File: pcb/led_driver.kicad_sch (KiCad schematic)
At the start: 60 parts, among them J1 48V IN, J2 LED, J3 12V IN, J4 INTERLOCK, Q1 IRF540N, SW3 ARM, U1 TC4427xOA, U2 74HC74, U3 74HC08, U4 LM393

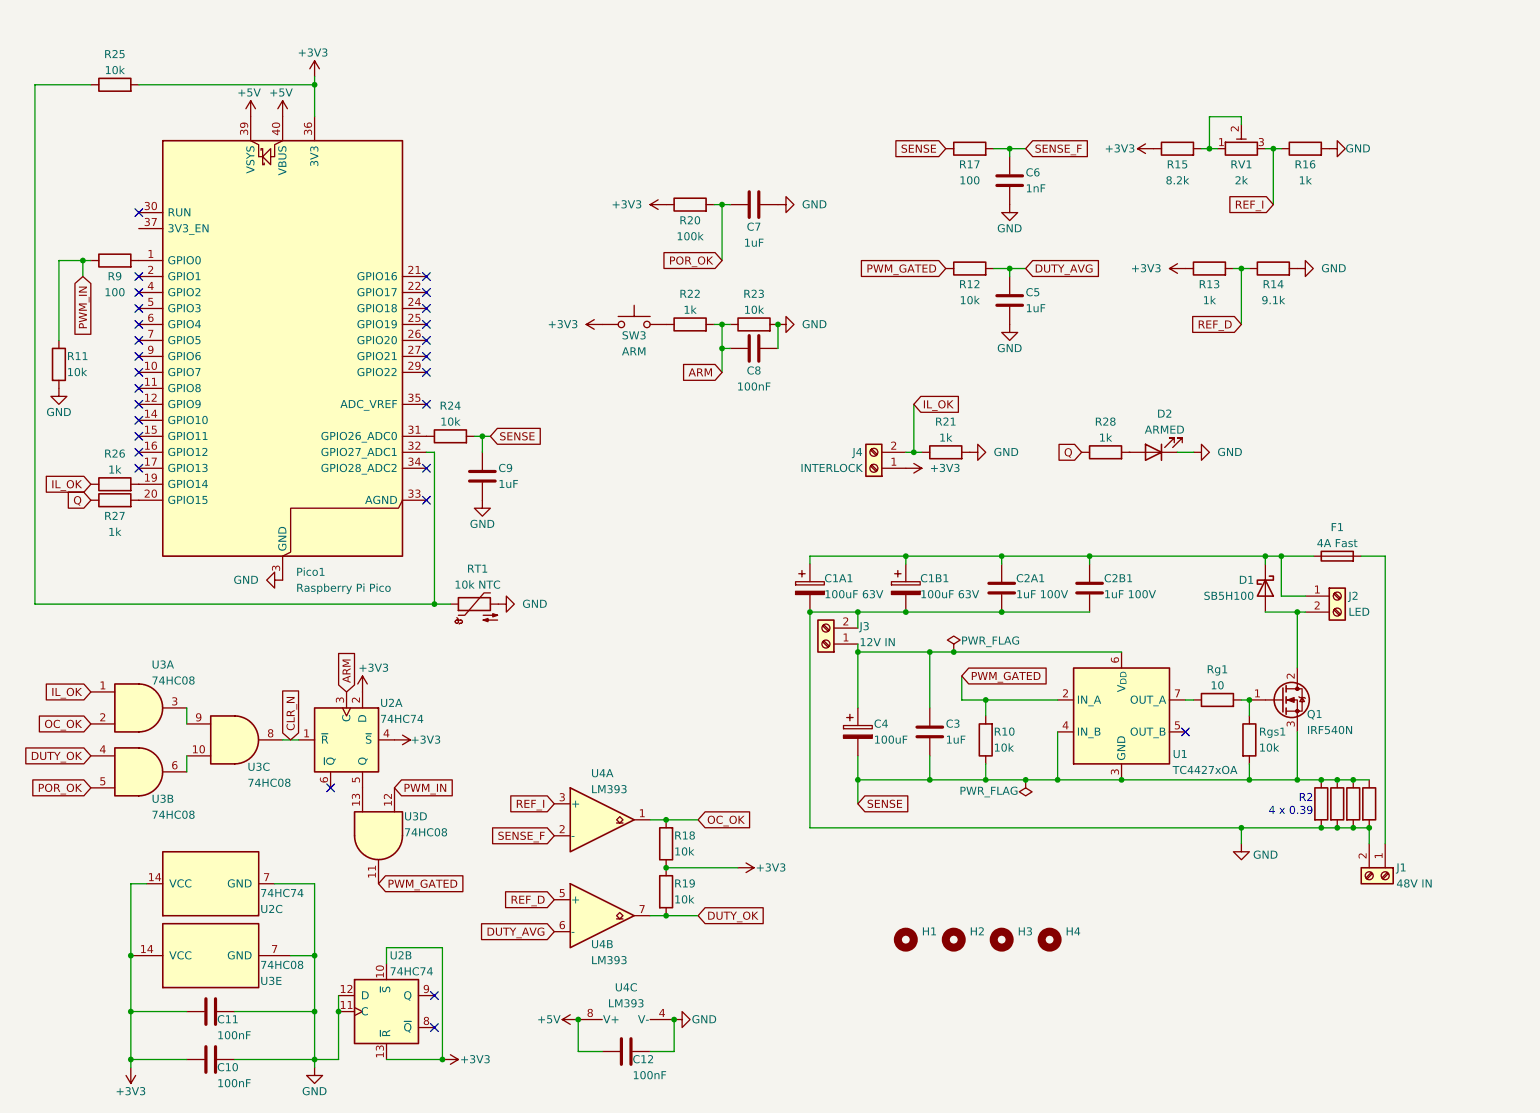
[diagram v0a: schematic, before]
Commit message: Initial routing for LED driver
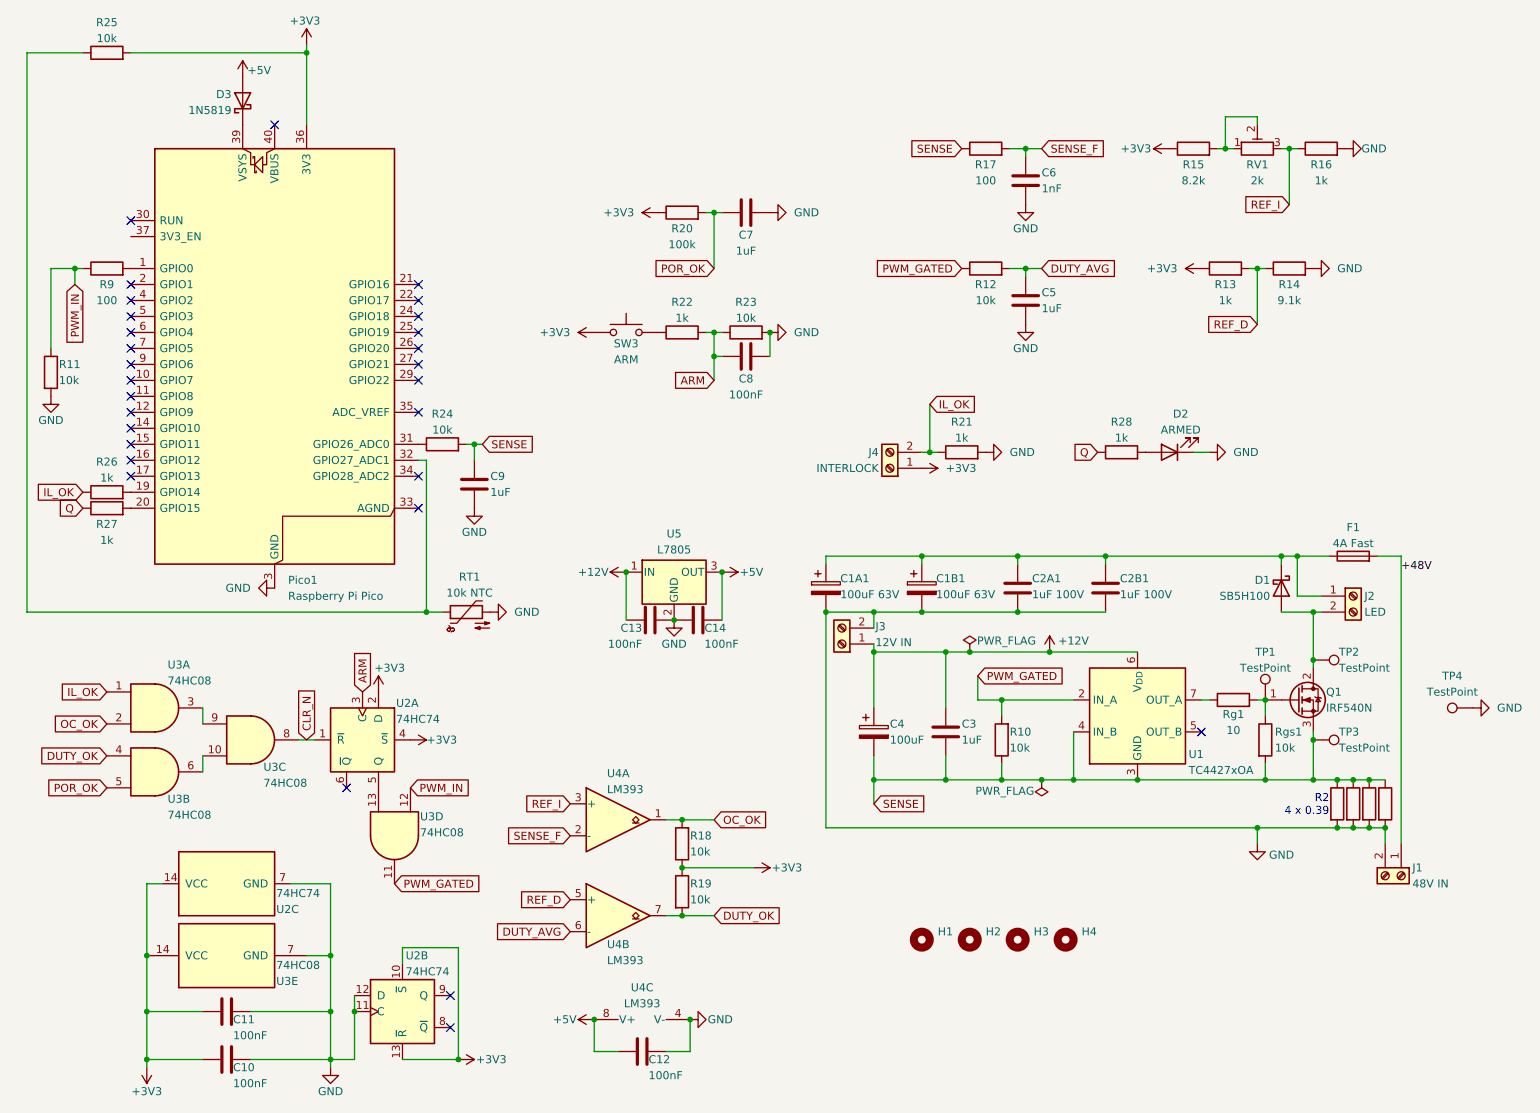
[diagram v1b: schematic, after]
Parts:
- added C13, C14: 100nF, Capacitor_THT:C_Rect_L7.2mm_W4.5mm_P5.00mm_FKS2_FKP2_MKS2_MKP2, symbol Device:C
- added D3: 1N5819, Diode_THT:D_DO-41_SOD81_P10.16mm_Horizontal, symbol Diode:1N5819
- added TP1, TP2, TP3, TP4: TestPoint, TestPoint:TestPoint_THTPad_D2.0mm_Drill1.0mm, symbol Connector:TestPoint
- added U5: L7805, Package_TO_SOT_THT:TO-220-3_Vertical, symbol Regulator_Linear:L7805
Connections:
- net +5V: now also C14.2, D3.2 (A), U5.3 (OUT); no longer Pico1.39 (VSYS), Pico1.40 (VBUS)
- net GND: now also C13.2, C14.1, TP4.1, U5.2 (GND)
- net SENSE: now also TP3.1
- net at Q1.1 (G), Rg1.2, Rgs1.1: now also TP1.1
- net at D1.2 (A), J2.2 (Pin_2), Q1.2 (D): now also TP2.1
- net +48V: now reaches F1.2, J1.1 (Pin_1)
- net +12V: now reaches C3.1, C4.1, J3.1 (Pin_1), U1.6 (V_{DD})
- net +12V: now also C13.1, U5.1 (IN)
- new net: D3.1 (K), Pico1.39 (VSYS)
- no-connect marks 28 -> 29
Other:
- moved on the sheet: C10, C11, C12, C1A1, C1B1, C2A1, C2B1, C3, C4, C5, C6, C7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

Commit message: Fix some constraint error and violations
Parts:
- added R29: 10k, Resistor_THT:R_Axial_DIN0207_L6.3mm_D2.5mm_P10.16mm_Horizontal, symbol Device:R
- Q1: value IRF540N -> STP30NF10
- R13: value 1k -> 10k
- R14: value 9.1k -> 8.2k
- Rgs1: footprint Resistor_THT:R_Axial_DIN0207_L6.3mm_D2.5mm_P10.16mm_Horizontal -> Resistor_THT:R_Axial_DIN0207_L6.3mm_D2.5mm_P2.54mm_Vertical
- U1: value TC4427xOA -> MIC4427
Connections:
- net DUTY_AVG: now also R29.1
- net GND: now also C3.2, C4.2, R10.1, U1.3 (GND), U1.4 (IN_B), R29.2
- net Q: now also U2.5 (Q), U3.13
- net SENSE: no longer C3.2, C4.2, R10.1, U1.3 (GND), U1.4 (IN_B)
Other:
- title: High-speed LED driver -> Fast-Switching LED Driver
- moved on the sheet: C5, R12, R13, R14, U3D

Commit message: First revision
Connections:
- net GND: now also Pico1.33 (AGND)
- net SENSE: no longer C9.1
- net at Pico1.31 (GPIO26_ADC0), R24.1: now also C9.1
- no-connect marks 29 -> 28
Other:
- moved on the sheet: C9, R24
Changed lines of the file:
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@@
 		(title "Fast-Switching LED Driver")
 		(date "2026-09-28")
-		(rev "0")
+		(rev "1")
 	)
 	(text "R2\n4 x 0.39"
@@
 	)
 	(junction
-		(at 111.76 83.82)
+		(at 109.22 83.82)
 		(diameter 0)
 		(color 0 0 0 0)
@@
 	)
 	(junction
-		(at 104.14 110.49)
+		(at 105.41 110.49)
 		(diameter 0)
 		(color 0 0 0 0)
@@
 	)
 	(no_connect
-		(at 102.87 93.98)
-	)
-	(no_connect
 		(at 57.15 81.28)
 	)
@@
 	(wire
 		(pts
-			(xy 102.87 86.36) (xy 104.14 86.36)
+			(xy 102.87 86.36) (xy 105.41 86.36)
 		)
 		(stroke
@@
 	(wire
 		(pts
+			(xy 109.22 83.82) (xy 109.22 86.36)
+		)
+		(stroke
+			(width 0)
+			(type default)
+		)
+	)
+	(wire
+		(pts
 			(xy 203.2 66.04) (xy 199.39 66.04)
 		)
@@
 	(wire
 		(pts
-			(xy 104.14 86.36) (xy 104.14 110.49)
+			(xy 105.41 86.36) (xy 105.41 110.49)
 		)
 		(stroke
@@
 	(wire
 		(pts
-			(xy 111.76 86.36) (xy 111.76 83.82)
-		)
-		(stroke
-			(width 0)
-			(type default)
-		)
-	)
-	(wire
-		(pts
 			(xy 231.14 31.75) (xy 236.22 31.75)
 		)
@@
 	(wire
 		(pts
-			(xy 104.14 110.49) (xy 106.68 110.49)
-		)
-		(stroke
-			(width 0)
-			(type default)
-		)
-	)
-	(wire
-		(pts
 			(xy 57.15 21.59) (xy 85.09 21.59)
 		)
@@
 	(wire
 		(pts
-			(xy 113.03 83.82) (xy 111.76 83.82)
-		)
-		(stroke
-			(width 0)
-			(type default)
-		)
-	)
-	(wire
-		(pts
 			(xy 207.01 137.16) (xy 217.17 137.16)
 		)
@@
 	(wire
 		(pts
-			(xy 111.76 83.82) (xy 110.49 83.82)
+			(xy 229.87 36.83) (xy 231.14 36.83)
 		)
 		(stroke
@@
 	(wire
 		(pts
-			(xy 229.87 36.83) (xy 231.14 36.83)
+			(xy 85.09 21.59) (xy 85.09 33.02)
 		)
 		(stroke
@@
 	(wire
 		(pts
-			(xy 85.09 21.59) (xy 85.09 33.02)
+			(xy 40.64 21.59) (xy 40.64 110.49)
 		)
 		(stroke
@@
 	(wire
 		(pts
-			(xy 40.64 21.59) (xy 40.64 110.49)
+			(xy 40.64 110.49) (xy 106.68 110.49)
 		)
 		(stroke
@@
 	(wire
 		(pts
-			(xy 40.64 110.49) (xy 104.14 110.49)
+			(xy 243.84 66.04) (xy 243.84 57.15)
 		)
 		(stroke
@@
 	(wire
 		(pts
-			(xy 243.84 66.04) (xy 243.84 57.15)
+			(xy 148.59 46.99) (xy 151.13 46.99)
 		)
 		(stroke
@@
 	(wire
 		(pts
-			(xy 148.59 46.99) (xy 151.13 46.99)
+			(xy 199.39 36.83) (xy 196.85 36.83)
 		)
 		(stroke
@@
 	(wire
 		(pts
-			(xy 199.39 36.83) (xy 196.85 36.83)
+			(xy 195.58 137.16) (xy 200.66 137.16)
 		)
 		(stroke
@@
 	(wire
 		(pts
-			(xy 195.58 137.16) (xy 200.66 137.16)
+			(xy 102.87 83.82) (xy 110.49 83.82)
 		)
 		(stroke
@@
 	(global_label "SENSE"
 		(shape input)
-		(at 113.03 83.82 0)
+		(at 118.11 83.82 0)
 		(fields_autoplaced yes)
 		(effects
@@
 		)
 		(property "Intersheetrefs" "${INTERSHEET_REFS}"
-			(at 122.0627 83.82 0)
+			(at 127.1427 83.82 0)
 			(hide yes)
 			(show_name no)
@@
 	(symbol
 		(lib_id "Device:C")
-		(at 111.76 90.17 0)
+		(at 109.22 90.17 0)
 		(unit 1)
 		(body_style 1)
@@
 		(dnp no)
 		(property "Reference" "C9"
-			(at 114.3 88.9 0)
+			(at 111.76 88.9 0)
 			(show_name no)
 			(do_not_autoplace no)
@@
 		)
 		(property "Value" "1uF"
-			(at 114.3 91.44 0)
+			(at 111.76 91.44 0)
 			(show_name no)
 			(do_not_autoplace no)
@@
 		)
 		(property "Footprint" "Capacitor_THT:C_Rect_L7.2mm_W4.5mm_P5.00mm_FKS2_FKP2_MKS2_MKP2"
-			(at 112.7252 93.98 0)
+			(at 110.1852 93.98 0)
 			(hide yes)
 			(show_name no)
@@
 		)
 		(property "Datasheet" ""
-			(at 111.76 90.17 0)
+			(at 109.22 90.17 0)
 			(hide yes)
 			(show_name no)
@@
 		)
 		(property "Description" "Unpolarized capacitor"
-			(at 111.76 90.17 0)
+			(at 109.22 90.17 0)
 			(hide yes)
 			(show_name no)
@@
 	(symbol
 		(lib_id "Device:R")
-		(at 106.68 83.82 90)
+		(at 114.3 83.82 90)
 		(unit 1)
 		(body_style 1)
@@
 		(dnp no)
 		(property "Reference" "R24"
-			(at 106.68 78.994 90)
+			(at 114.3 78.994 90)
 			(show_name no)
 			(do_not_autoplace no)
@@
 		)
 		(property "Value" "10k"
-			(at 106.68 81.534 90)
+			(at 114.3 81.534 90)
 			(show_name no)
 			(do_not_autoplace no)
@@
 		)
 		(property "Footprint" "Resistor_THT:R_Axial_DIN0207_L6.3mm_D2.5mm_P10.16mm_Horizontal"
-			(at 106.68 85.598 90)
+			(at 114.3 85.598 90)
 			(hide yes)
 			(show_name no)
@@
 		)
 		(property "Datasheet" ""
-			(at 106.68 83.82 0)
+			(at 114.3 83.82 0)
 			(hide yes)
 			(show_name no)
@@
 		)
 		(property "Description" "Resistor"
-			(at 106.68 83.82 0)
+			(at 114.3 83.82 0)
 			(hide yes)
 			(show_name no)
@@
 	)
 	(symbol
+		(lib_id "power:GND")
+		(at 102.87 93.98 0)
+		(unit 1)
+		(body_style 1)
+		(exclude_from_sim no)
+		(in_bom yes)
+		(on_board yes)
+		(in_pos_files yes)
+		(dnp no)
+		(property "Reference" "#PWR035"
+			(at 102.87 100.33 0)
+			(hide yes)
+			(show_name no)
+			(do_not_autoplace no)
+			(effects
+				(font
+					(size 1.27 1.27)
+				)
+			)
+		)
+		(property "Value" "GND"
+			(at 102.87 97.79 0)
+			(show_name no)
+			(do_not_autoplace no)
+			(effects
+				(font
+					(size 1.27 1.27)
+				)
+			)
+		)
+		(property "Footprint" ""
+			(at 102.87 93.98 0)
+			(hide yes)
+			(show_name no)
+			(do_not_autoplace no)
+			(effects
+				(font
+					(size 1.27 1.27)
+				)
+			)
+		)
+		(property "Datasheet" ""
+			(at 102.87 93.98 0)
+			(hide yes)
+			(show_name no)
+			(do_not_autoplace no)
+			(effects
+				(font
+					(size 1.27 1.27)
+				)
+			)
+		)
+		(property "Description" "Power symbol creates a global label with name \"GND\" , ground"
+			(at 102.87 93.98 0)
+			(hide yes)
+			(show_name no)
+			(do_not_autoplace no)
+			(effects
+				(font
+					(size 1.27 1.27)
+				)
+			)
+		)
+		(pin "1"
+		)
+		(instances
+			(project "led_driver"
+				(path "/517fb8ba-efa2-4ff9-8737-3053492b2e56"
+					(reference "#PWR035")
+					(unit 1)
+				)
+			)
+		)
+	)
+	(symbol
 		(lib_id "Connector:Screw_Terminal_01x02")
 		(at 259.08 152.4 270)
@@
 	(symbol
 		(lib_id "power:GND")
-		(at 111.76 93.98 0)
+		(at 109.22 93.98 0)
 		(unit 1)
 		(body_style 1)
@@
 		(dnp no)
 		(property "Reference" "#PWR023"
-			(at 111.76 100.33 0)
+			(at 109.22 100.33 0)
 			(hide yes)
 			(show_name no)
@@
 		)
 		(property "Value" "GND"
-			(at 111.76 97.79 0)
+			(at 109.22 97.79 0)
 			(show_name no)
 			(do_not_autoplace no)
@@
 		)
 		(property "Footprint" ""
-			(at 111.76 93.98 0)
+			(at 109.22 93.98 0)
 			(hide yes)
 			(show_name no)
@@
 		)
 		(property "Datasheet" ""
-			(at 111.76 93.98 0)
+			(at 109.22 93.98 0)
 			(hide yes)
 			(show_name no)
@@
 		)
 		(property "Description" "Power symbol creates a global label with name \"GND\" , ground"
-			(at 111.76 93.98 0)
+			(at 109.22 93.98 0)
 			(hide yes)
 			(show_name no)
